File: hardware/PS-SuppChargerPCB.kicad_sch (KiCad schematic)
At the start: 0 parts

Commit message: very basic power arch
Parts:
- added C1, C11, C12, C3, C5, C6: 100nF, symbol Device:C
- added C10, C2, C7, C9: 80uF, symbol Device:C
- added C13, C4: 470nF, symbol Device:C
- added C14, C8: Csys, symbol Device:C
- added C15, C16: 4.7uF, symbol Device:C
- added C17: 1uF, symbol Device:C
- added L1: 10uH, symbol Device:L
- added Q1, Q2, Q3, Q4: SiR880BDP, Package_SO:PowerPAK_SO-8_Single, symbol Transistor_FET:Si7336ADP
- added R1, R2, R5, R6: 10, symbol Device:R_US
- added R10: 9.42k, symbol Device:R_US
- added R11: 249k, symbol Device:R_US
- added R12: 5.24k, symbol Device:R_US
- added R13: 30.31k, symbol Device:R_US
- added R3, R4: 5m, symbol Device:R_US
- added R7: 57.1k, symbol Device:R_US
- added R8: 10k, symbol Device:R_US
- added R9: 3k, symbol Device:R_US
- added U1: BQ25756ERRVR, VQFN36_RRV_TEX, symbol SuppCharger:BQ25756ERRVR
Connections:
- new net: C4.1, C5.1, R2.2, U1.13 (SRN)
- new net: C4.2, C6.2, R1.2, U1.14 (SRP)
- new net: Q4.4 (G), U1.19 (HIDRV2)
- new net: C3.1, U1.20 (BTST2)
- new net: Q3.4 (G), U1.21 (LODRV2)
- new net: Q2.4 (G), U1.25 (LODRV1)
- new net: C1.1, U1.26 (BTST1)
- new net: Q1.4 (G), U1.27 (HIDRV1)
- new net: C1.2, L1.1, Q1.1 (S), Q1.2 (S), Q1.3 (S), Q2.5 (D), U1.28 (SW1)
- new net: C9.2, Q1.5 (D), R4.2, R5.1
- new net ACN: C11.1, C13.1, R5.2
- new net ACP: C12.2, C13.2, R6.2
- new net ACUV: C10.1, C17.2, R4.1, R6.1, U1.33 (VAC), U1.34 (ACUV)
- new net Battery: C14.1, C2.1, Q4.1 (S), Q4.2 (S), Q4.3 (S), R11.1, R2.1, R3.2
- new net Battery Mid: R12.2, R13.1, U1.8 (TS)
- new net DRV_SUP: C16.1, U1.23 (DRV_SUP)
- new net FB: R10.1, R11.2, U1.12 (FB)
- new net FBG: R10.2, U1.11 (FBG)
- new net FSW_SYNC: R7.1, U1.36 (FSW_SYNC)
- new net GND: C10.2, C11.2, C12.1, C14.2, C15.2, C16.2, C17.1, C2.2, C5.2, C6.1, C7.2, C8.2, C9.1, Q2.1 (S), Q2.2 (S), Q2.3 (S), Q3.5 (D), R13.2, R7.2, R8.2, R9.2, U1.17 (PGND), U1.35 (ACOV), U1.7 (*CE)
- new net ICHG: R8.1, U1.9 (ICHG)
- new net ILIM_HIZ: R9.1, U1.10 (ILIM_HIZ)
- new net REGN: C15.1, R12.1, U1.24 (REGN)
- new net SW2: C3.2, L1.2, Q3.1 (S), Q3.2 (S), Q3.3 (S), Q4.5 (D), U1.18 (SW2)
- new net System: C7.1, C8.1, R1.1, R3.1
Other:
- note added: "Buck"
- note added: "TSP2663x"

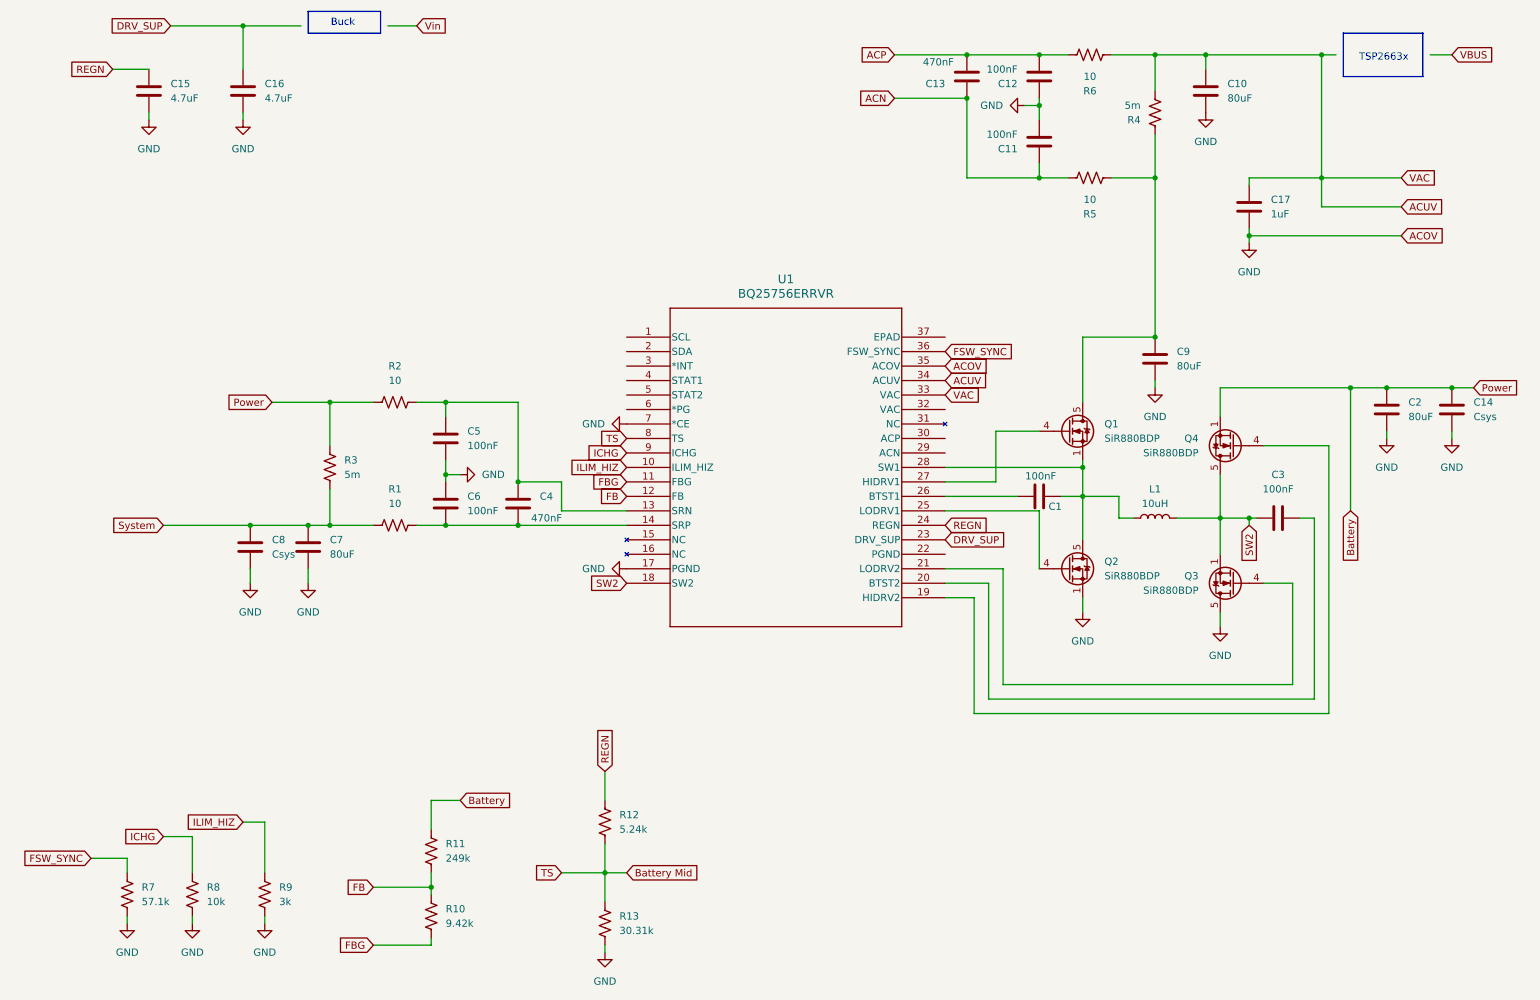
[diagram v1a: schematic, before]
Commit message: switching logic for buck boost completed mosfet + inductor selected
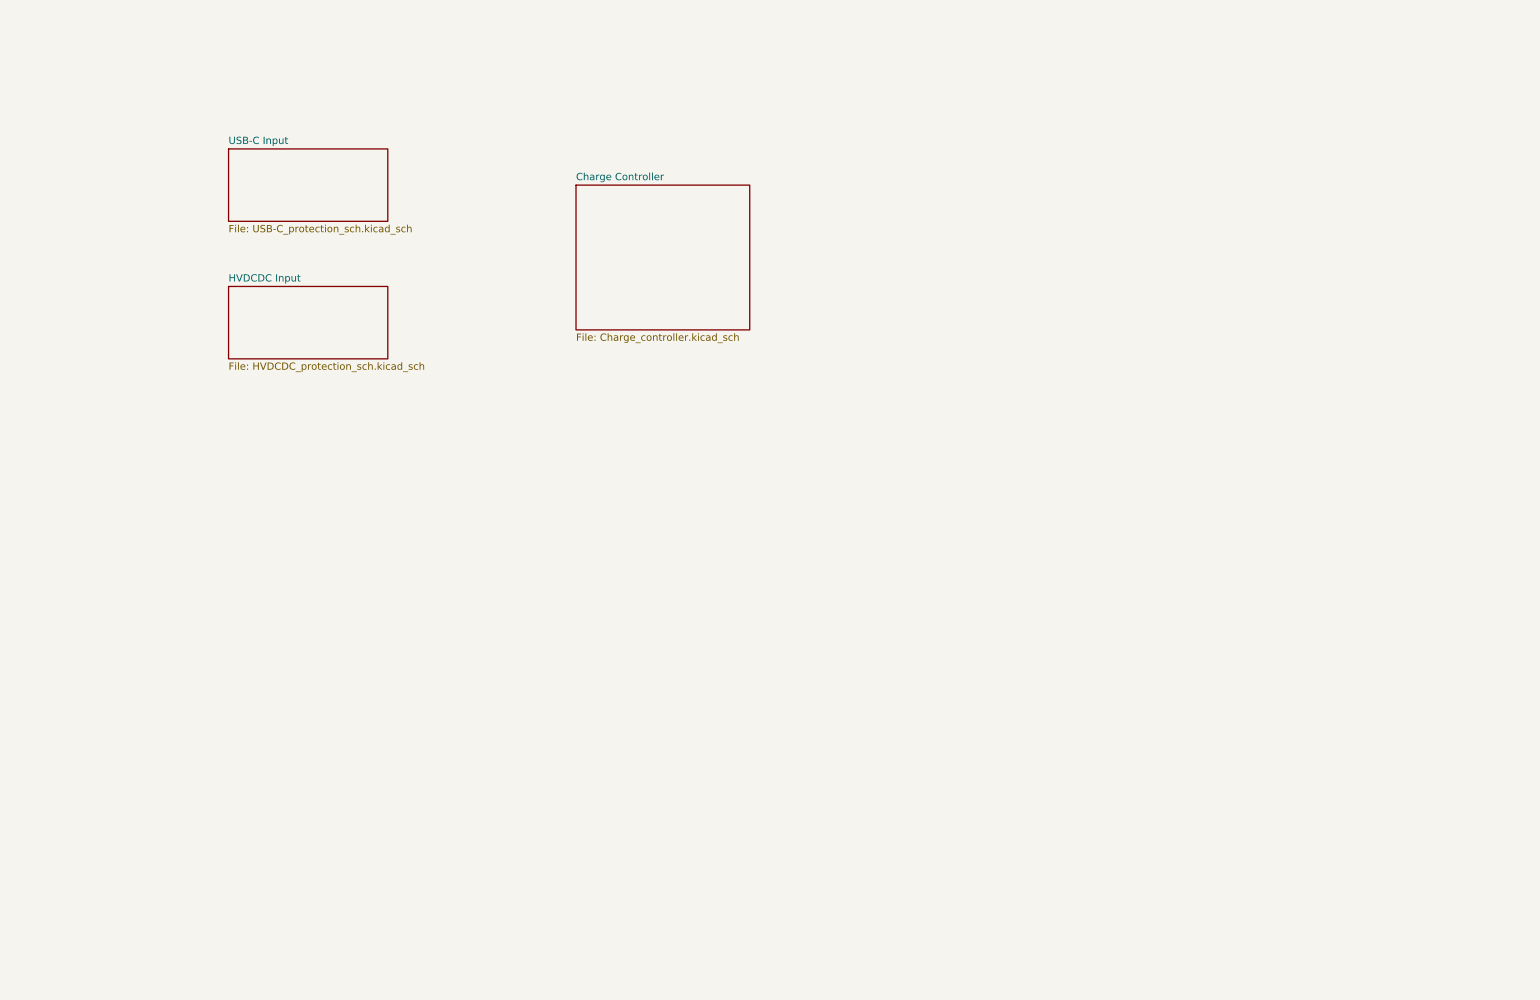
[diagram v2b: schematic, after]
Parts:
- removed C1, C11, C12, C3, C5, C6: 100nF, symbol Device:C
- removed C10, C2, C7, C9: 80uF, symbol Device:C
- removed C13, C4: 470nF, symbol Device:C
- removed C14, C8: Csys, symbol Device:C
- removed C15, C16: 4.7uF, symbol Device:C
- removed C17: 1uF, symbol Device:C
- removed L1: 10uH, symbol Device:L
- removed Q1, Q2, Q3, Q4: SiR880BDP, Package_SO:PowerPAK_SO-8_Single, symbol Transistor_FET:Si7336ADP
- removed R1, R2, R5, R6: 10, symbol Device:R_US
- removed R10: 9.42k, symbol Device:R_US
- removed R11: 249k, symbol Device:R_US
- removed R12: 5.24k, symbol Device:R_US
- removed R13: 30.31k, symbol Device:R_US
- removed R3, R4: 5m, symbol Device:R_US
- removed R7: 57.1k, symbol Device:R_US
- removed R8: 10k, symbol Device:R_US
- removed R9: 3k, symbol Device:R_US
- removed U1: BQ25756ERRVR, VQFN36_RRV_TEX, symbol SuppCharger:BQ25756ERRVR
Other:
- added sheet Charge Controller (Charge_controller.kicad_sch)
- added sheet HVDCDC Input (HVDCDC_protection_sch.kicad_sch)
- added sheet USB-C Input (USB-C_protection_sch.kicad_sch)
- note removed: "Buck"
- note removed: "TSP2663x"
- company: (none) -> Kell Harpole LHRS
- title: (none) -> Supp Charger
